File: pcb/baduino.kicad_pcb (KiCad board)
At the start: 2 copper layers, 30 x 17.2 mm, 24 parts, among them J1 USB_A, J3 TF-015, SW1 SW_DIP_x04, U1 ATmega32U4-M, U2 MIC5219-3.3YM5, X1 ASE-xxxMHz

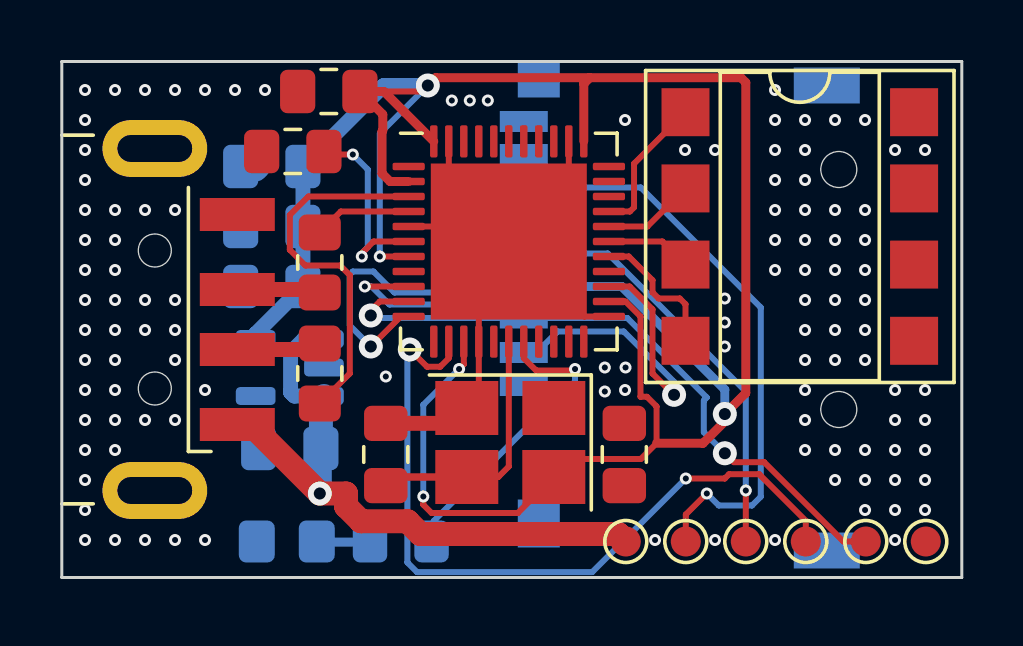
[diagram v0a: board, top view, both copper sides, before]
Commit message: switch to non powered crystal oscillator
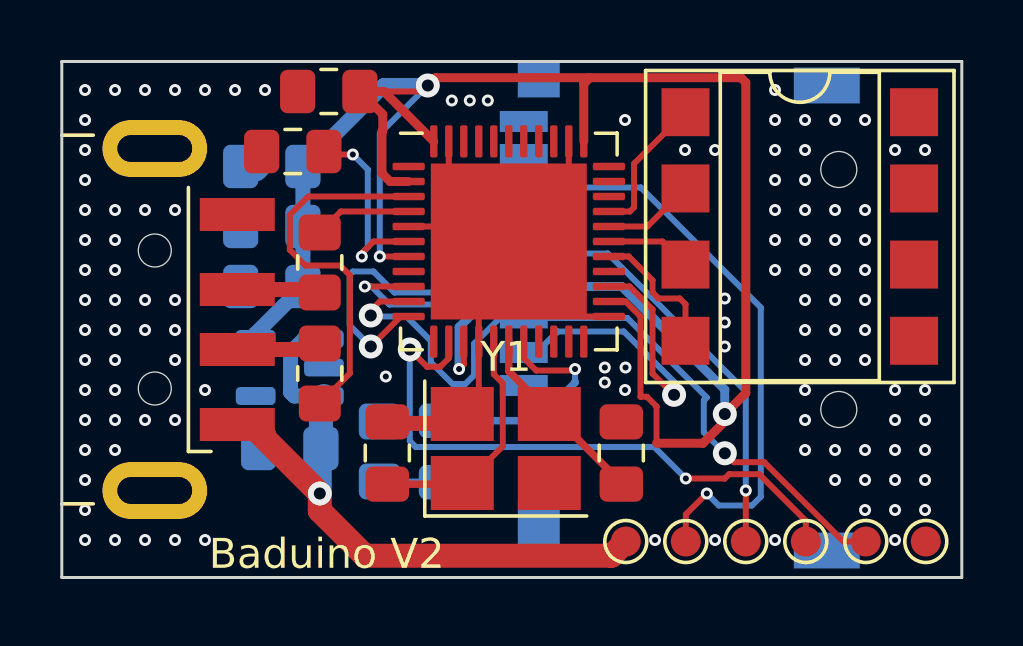
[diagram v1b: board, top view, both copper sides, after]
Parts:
- removed X1: ASE-xxxMHz, Crystal:Crystal_SMD_3225-4Pin_3.2x2.5mm_HandSoldering
- added Y1: Crystal_GND24, Crystal:Crystal_SMD_3225-4Pin_3.2x2.5mm_HandSoldering, F.Cu at (72.6, 103.5)
- moved C1 7.90 mm to (68.7, 103.7), turned to -90 degrees
- moved C2 7.85 mm to (76.5, 103.7)
- moved R3 4.31 mm to (68.4, 103.6), turned to 90 degrees
- moved D1 3.27 mm to (70.4, 103.6), turned to 90 degrees
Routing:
- net +3.3V: track 85.4 -> 75.6 mm, vias 5 -> 4
- net XTAL2: track 0.00 -> 7.98 mm
- net RST: track 25.4 -> 20.5 mm
- net MOSI: track 21.9 -> 25.0 mm
- net Net-(D1-A): track 10.2 -> 7.93 mm
- net XTAL1: track 8.53 -> 6.37 mm
